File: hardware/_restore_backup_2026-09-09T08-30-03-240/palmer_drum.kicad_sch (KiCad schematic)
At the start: 13 parts, among them J1 EURO_PWR, J2 SERGE_PWR, U3 L7805

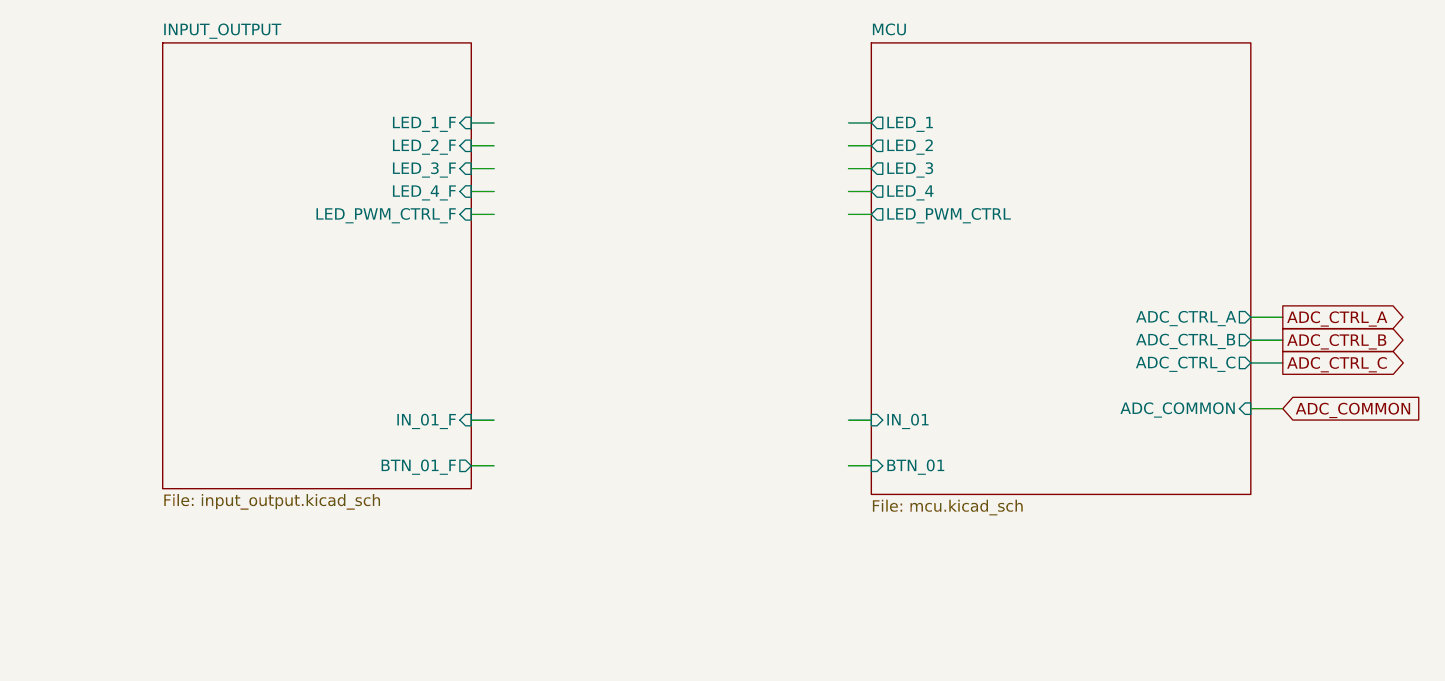
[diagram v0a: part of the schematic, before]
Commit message: Updated schematic to handle led pwm brightness control
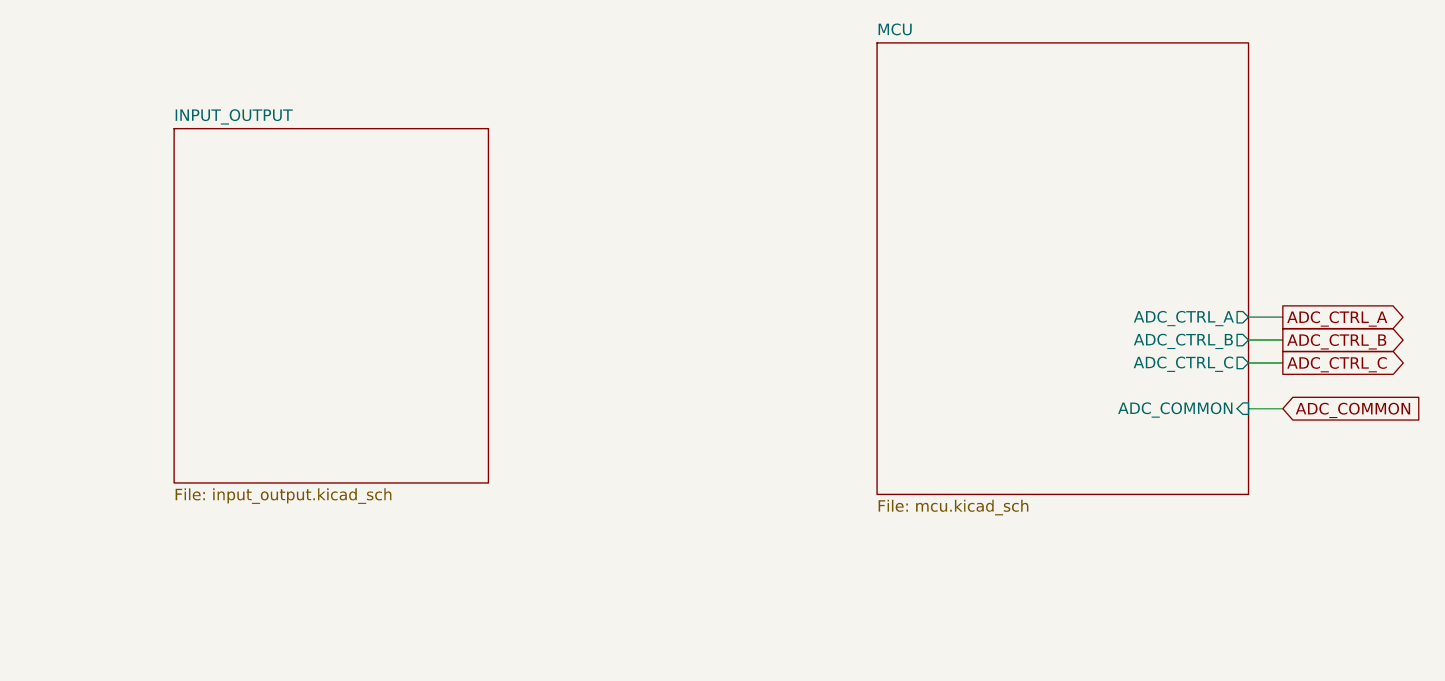
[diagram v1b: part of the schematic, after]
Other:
- sheet INPUT_OUTPUT ports: added none; removed BTN_01_F, IN_01_F, LED_1_F, LED_2_F, LED_3_F, LED_4_F, LED_PWM_CTRL_F
- sheet MCU ports: added none; removed BTN_01, IN_01, LED_1, LED_2, LED_3, LED_4, LED_PWM_CTRL
